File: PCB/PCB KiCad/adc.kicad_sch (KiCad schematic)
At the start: 10 parts, among them U2 NAU7802SGI, U4 LP5951MFX-1.8_NOPB

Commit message: Minor schematic cleanup!
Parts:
- removed U4: LP5951MFX-1.8_NOPB, LP5951MFX-1.8_NOPB:SOT95P280X145-5N, symbol LP5951MFX-1.8_NOPB:LP5951MFX-1.8_NOPB
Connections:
- net +3V3 is gone; now on net +3.3V: C10.1, U2.15 (DVDD), U2.16 (AVDD/LDO)
- net +3.3V: now reaches R6.2
- net DRDY_INT: now reaches U2.12 (DRDY)
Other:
- moved on the sheet: C10, C11, C6, C7, C8, C9, R5, R6, U2

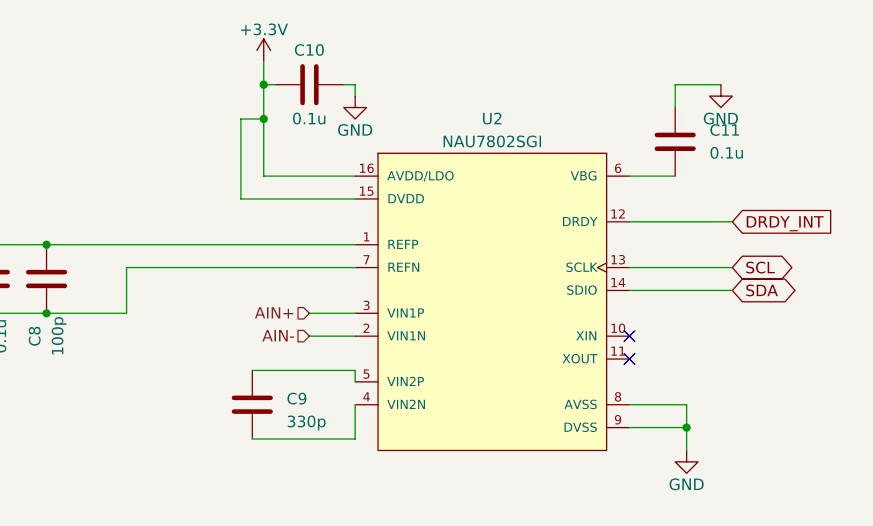
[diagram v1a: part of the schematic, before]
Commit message: Giant schematic cleanup to make more sense of the sensor circuit and just clean everything up a bit.
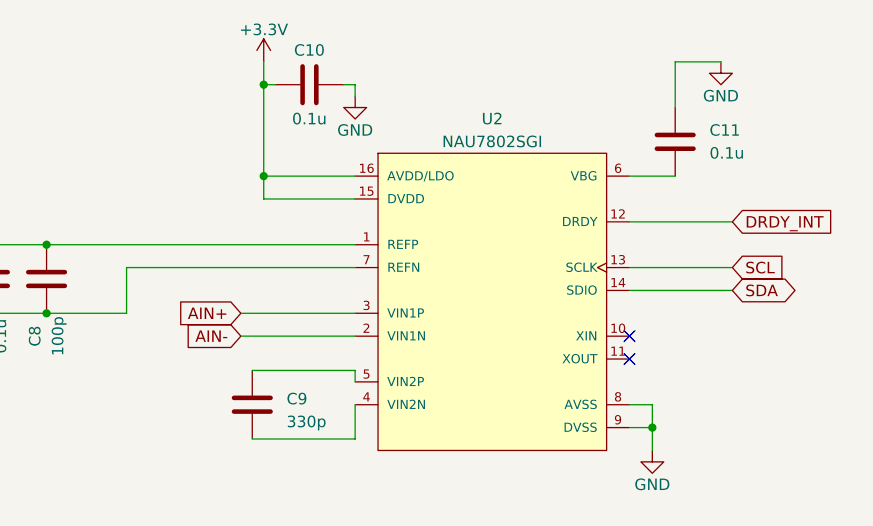
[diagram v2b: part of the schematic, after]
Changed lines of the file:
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@@
 	)
 	(junction
-		(at 173.99 118.11)
+		(at 127 90.17)
 		(diameter 0)
 		(color 0 0 0 0)
 	)
 	(junction
-		(at 127 83.82)
+		(at 170.18 118.11)
 		(diameter 0)
 		(color 0 0 0 0)
@@
 	(wire
 		(pts
-			(xy 167.64 118.11) (xy 173.99 118.11)
+			(xy 167.64 118.11) (xy 170.18 118.11)
 		)
 		(stroke
@@
 	(wire
 		(pts
-			(xy 132.08 107.95) (xy 137.16 107.95)
+			(xy 124.46 107.95) (xy 137.16 107.95)
 		)
 		(stroke
@@
 	(wire
 		(pts
-			(xy 173.99 115.57) (xy 173.99 118.11)
+			(xy 170.18 115.57) (xy 170.18 118.11)
+		)
+		(stroke
+			(width 0)
+			(type default)
+		)
+	)
+	(wire
+		(pts
+			(xy 127 90.17) (xy 127 92.71)
 		)
 		(stroke
@@
 	(wire
 		(pts
-			(xy 127 83.82) (xy 124.46 83.82)
-		)
-		(stroke
-			(width 0)
-			(type default)
-		)
-	)
-	(wire
-		(pts
 			(xy 137.16 100.33) (xy 111.76 100.33)
 		)
@@
 	(wire
 		(pts
-			(xy 127 83.82) (xy 127 80.01)
-		)
-		(stroke
-			(width 0)
-			(type default)
-		)
-	)
-	(wire
-		(pts
 			(xy 90.17 85.09) (xy 90.17 87.63)
 		)
@@
 	(wire
 		(pts
-			(xy 172.72 80.01) (xy 172.72 82.55)
-		)
-		(stroke
-			(width 0)
-			(type default)
-		)
-	)
-	(wire
-		(pts
-			(xy 124.46 83.82) (xy 124.46 92.71)
-		)
-		(stroke
-			(width 0)
-			(type default)
-		)
-	)
-	(wire
-		(pts
-			(xy 177.8 80.01) (xy 172.72 80.01)
+			(xy 172.72 77.47) (xy 172.72 82.55)
+		)
+		(stroke
+			(width 0)
+			(type default)
+		)
+	)
+	(wire
+		(pts
+			(xy 177.8 77.47) (xy 172.72 77.47)
 		)
 		(stroke
@@
 	(wire
 		(pts
-			(xy 127 83.82) (xy 127 90.17)
+			(xy 127 80.01) (xy 127 90.17)
 		)
 		(stroke
@@
 	(wire
 		(pts
-			(xy 132.08 105.41) (xy 137.16 105.41)
+			(xy 124.46 105.41) (xy 137.16 105.41)
 		)
 		(stroke
@@
 	(wire
 		(pts
-			(xy 167.64 115.57) (xy 173.99 115.57)
-		)
-		(stroke
-			(width 0)
-			(type default)
-		)
-	)
-	(wire
-		(pts
-			(xy 173.99 118.11) (xy 173.99 120.65)
+			(xy 167.64 115.57) (xy 170.18 115.57)
+		)
+		(stroke
+			(width 0)
+			(type default)
+		)
+	)
+	(wire
+		(pts
+			(xy 170.18 118.11) (xy 170.18 120.65)
 		)
 		(stroke
@@
 	(wire
 		(pts
-			(xy 124.46 92.71) (xy 137.16 92.71)
-		)
-		(stroke
-			(width 0)
-			(type default)
-		)
-	)
-	(wire
-		(pts
 			(xy 137.16 80.01) (xy 137.16 81.28)
 		)
@@
 		)
 	)
+	(wire
+		(pts
+			(xy 127 92.71) (xy 137.16 92.71)
+		)
+		(stroke
+			(width 0)
+			(type default)
+		)
+	)
 	(global_label "SCL"
-		(shape bidirectional)
+		(shape input)
 		(at 179.07 100.33 0)
 		(fields_autoplaced yes)
@@
 		)
 		(property "Intersheetrefs" "${INTERSHEET_REFS}"
-			(at 184.9907 100.2506 0)
+			(at 185.5628 100.33 0)
 			(effects
 				(font
@@
 		)
 	)
+	(global_label "AIN-"
+		(shape input)
+		(at 124.46 107.95 180)
+		(fields_autoplaced yes)
+		(effects
+			(font
+				(size 1.27 1.27)
+			)
+			(justify right)
+		)
+		(property "Intersheetrefs" "${INTERSHEET_REFS}"
+			(at 116.8785 107.95 0)
+			(effects
+				(font
+					(size 1.27 1.27)
+				)
+				(justify right)
+				(hide yes)
+			)
+		)
+	)
+	(global_label "AIN+"
+		(shape input)
+		(at 124.46 105.41 180)
+		(fields_autoplaced yes)
+		(effects
+			(font
+				(size 1.27 1.27)
+			)
+			(justify right)
+		)
+		(property "Intersheetrefs" "${INTERSHEET_REFS}"
+			(at 116.8785 105.41 0)
+			(effects
+				(font
+					(size 1.27 1.27)
+				)
+				(justify right)
+				(hide yes)
+			)
+		)
+	)
 	(global_label "DRDY_INT"
 		(shape input)
@@
 				(hide yes)
 			)
-		)
-	)
-	(hierarchical_label "AIN+"
-		(shape input)
-		(at 132.08 105.41 180)
-		(effects
-			(font
-				(size 1.27 1.27)
-			)
-			(justify right)
-		)
-	)
-	(hierarchical_label "AIN-"
-		(shape input)
-		(at 132.08 107.95 180)
-		(effects
-			(font
-				(size 1.27 1.27)
-			)
-			(justify right)
 		)
 	)
@@
 	(symbol
 		(lib_id "power:GND")
-		(at 177.8 80.01 0)
+		(at 177.8 77.47 0)
 		(mirror y)
 		(unit 1)
@@
 		(dnp no)
 		(property "Reference" "#PWR8"
-			(at 177.8 86.36 0)
+			(at 177.8 83.82 0)
 			(effects
 				(font
@@
 		)
 		(property "Value" "GND"
-			(at 177.8 83.82 0)
+			(at 177.8 81.28 0)
 			(effects
 				(font
@@
 		)
 		(property "Footprint" ""
-			(at 177.8 80.01 0)
+			(at 177.8 77.47 0)
 			(effects
 				(font
@@
 		)
 		(property "Datasheet" ""
-			(at 177.8 80.01 0)
+			(at 177.8 77.47 0)
 			(effects
 				(font
@@
 		)
 		(property "Description" "Power symbol creates a global label with name \"GND\" , ground"
-			(at 177.8 80.01 0)
+			(at 177.8 77.47 0)
 			(effects
 				(font
@@
 	(symbol
 		(lib_id "power:GND")
-		(at 173.99 120.65 0)
+		(at 170.18 120.65 0)
 		(unit 1)
 		(exclude_from_sim no)
@@
 		(dnp no)
 		(property "Reference" "#PWR9"
-			(at 173.99 127 0)
+			(at 170.18 127 0)
 			(effects
 				(font
@@
 		)
 		(property "Value" "GND"
-			(at 173.99 124.46 0)
+			(at 170.18 124.46 0)
 			(effects
 				(font
@@
 		)
 		(property "Footprint" ""
-			(at 173.99 120.65 0)
+			(at 170.18 120.65 0)
 			(effects
 				(font
@@
 		)
 		(property "Datasheet" ""
-			(at 173.99 120.65 0)
+			(at 170.18 120.65 0)
 			(effects
 				(font
@@
 		)
 		(property "Description" "Power symbol creates a global label with name \"GND\" , ground"
-			(at 173.99 120.65 0)
-			(effects
-				(font
+			(at 170.18 120.65 0)
+			(effects
+				(font
